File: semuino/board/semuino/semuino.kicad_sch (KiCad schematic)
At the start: 56 parts, among them J1 12V_POWER_IN, J10 POW LED 3, J11 RF ON/OFF, J12 Screen, J13 Earth humidity sensor, J14 Select, J2 Select, J3 12V_POWER_OUT, J4 5V_POWER_IN, J5 RGB 1, J6 RGB 2, J7 RGB 3, J8 POW LED 1, J9 POW LED 2, Q1 2N2222A, Q2 P03P4L-04, Q3 2N2222A, Q4 2N2222A, Q5 2N2222A, Q6 P03P4L-04, Q7 P03P4L-04, Q8 P03P4L-04, U1 RtcArduino, U2 BPC_ESP8266-01_ESP-01, U3 BPC_DHT22, U4 BPC_Alim3_3V

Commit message: Après nettoyage et vérification des règles
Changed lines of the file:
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@@
   (junction (at 39.37 19.05) (diameter 0) (color 0 0 0 0)
   )
+  (junction (at 52.07 19.05) (diameter 0) (color 0 0 0 0)
+  )
   (junction (at 250.19 115.57) (diameter 0) (color 0 0 0 0)
   )
@@
     (stroke (width 0) (type default))
   )
+  (wire (pts (xy 52.07 17.78) (xy 52.07 19.05))
+    (stroke (width 0) (type default))
+  )
   (wire (pts (xy 66.04 124.46) (xy 58.42 124.46))
     (stroke (width 0) (type default))
@@
     (stroke (width 0) (type default))
   )
+  (wire (pts (xy 52.07 19.05) (xy 77.47 19.05))
+    (stroke (width 0) (type default))
+  )
   (wire (pts (xy 58.42 109.22) (xy 66.04 109.22))
     (stroke (width 0) (type default))
@@
     (stroke (width 0) (type default))
   )
-  (wire (pts (xy 39.37 19.05) (xy 77.47 19.05))
+  (wire (pts (xy 39.37 19.05) (xy 52.07 19.05))
     (stroke (width 0) (type default))
   )
@@
         )
       )
+    )
+  )
+  (symbol (lib_id "power:PWR_FLAG") (at 52.07 17.78 0) (unit 1)
+    (in_bom yes) (on_board yes) (dnp no) (fields_autoplaced)
+    (property "Reference" "#FLG01" (at 52.07 15.875 0)
+      (effects (font (size 1.27 1.27)) hide)
+    )
+    (property "Value" "PWR_FLAG" (at 52.07 13.835 0)
+      (effects (font (size 1.27 1.27)))
+    )
+    (property "Footprint" "" (at 52.07 17.78 0)
+      (effects (font (size 1.27 1.27)) hide)
+    )
+    (property "Datasheet" "~" (at 52.07 17.78 0)
+      (effects (font (size 1.27 1.27)) hide)
+    )
+    (pin "1")
+    (instances
+      (project "semuino"
+        (path "/9b55b725-5036-433a-9024-8e2d1f50e0ac"
+          (reference "#FLG01") (unit 1)
+        )
+      )

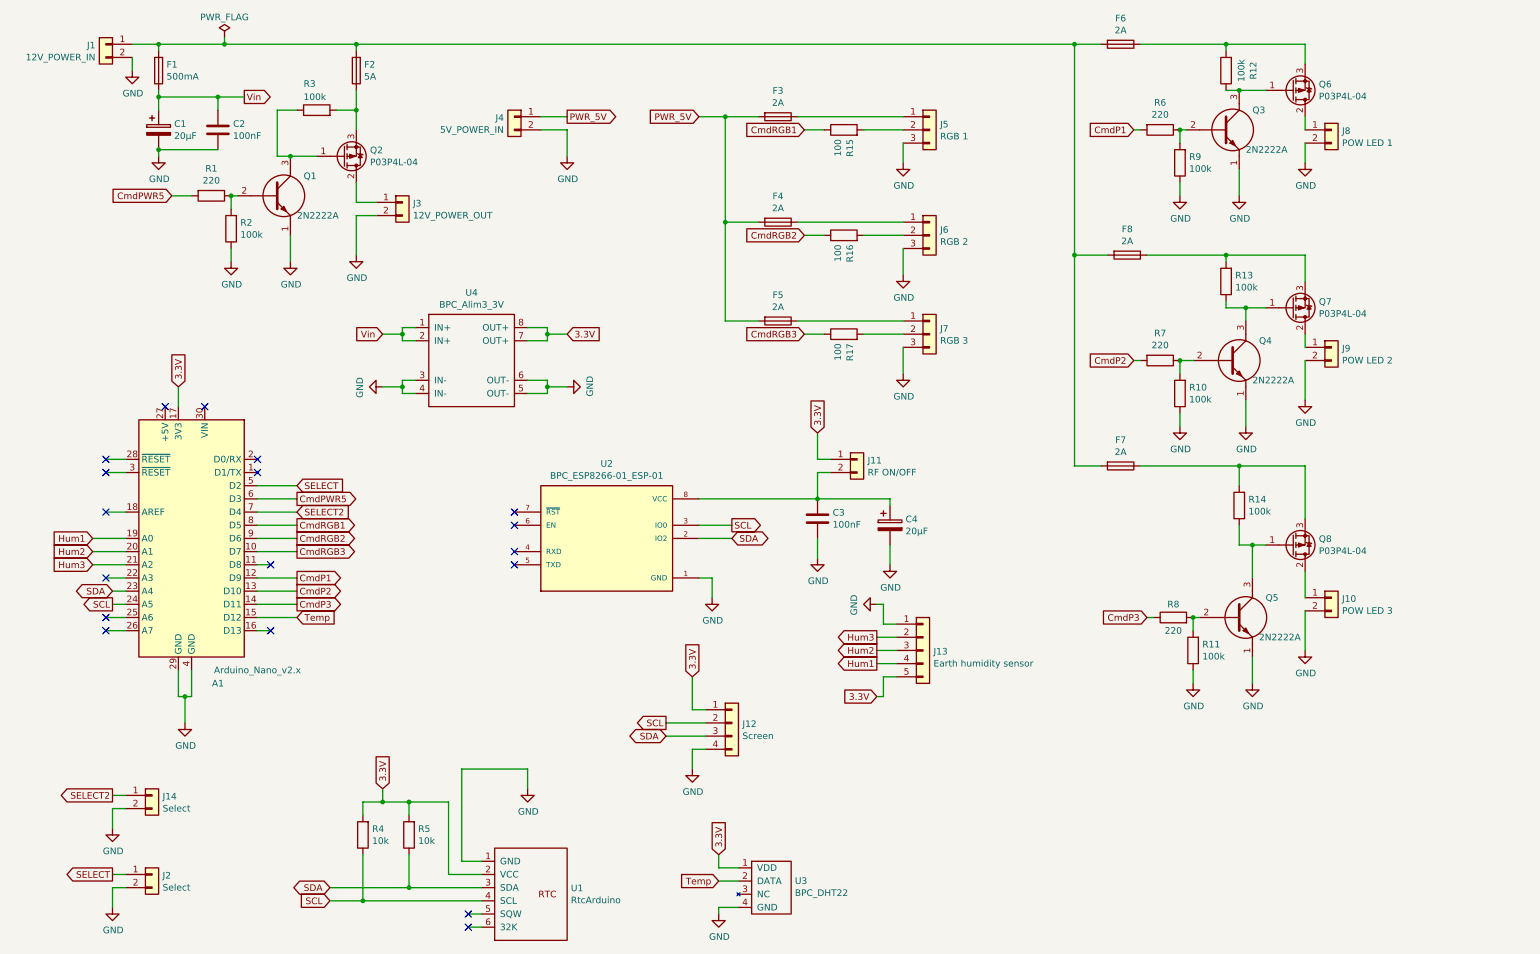
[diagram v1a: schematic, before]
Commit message: Modification valeur des résistances de commande + Marquage future A1
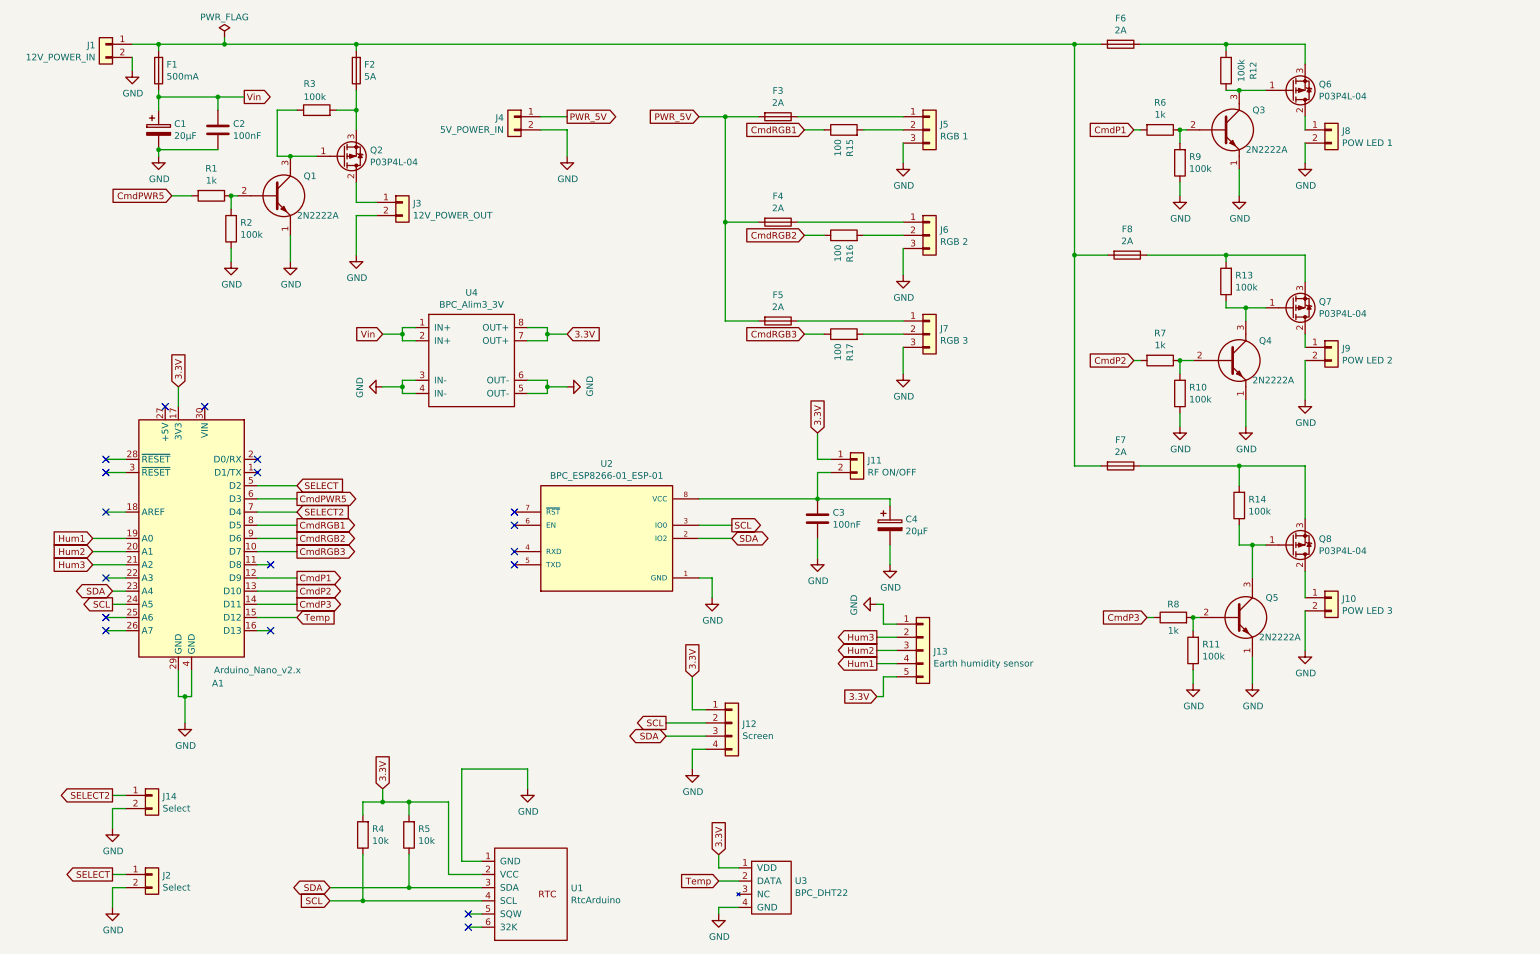
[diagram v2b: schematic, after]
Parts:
- R1, R6, R7, R8: value 220 -> 1k
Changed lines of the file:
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@@
   (title_block
     (title "Semuino - Contrôleur de meuble à semis")
-    (date "2023-09-21")
-    (rev "A0")
+    (date "2023-10-18")
+    (rev "A1")
     (company "BPC")
     (comment 2 "Température ambiante - 3 Capteurs d'humidité")
@@
       (effects (font (size 1.27 1.27)))
     )
-    (property "Value" "220" (at 232.41 32.6136 90)
+    (property "Value" "1k" (at 232.41 32.6136 90)
       (effects (font (size 1.27 1.27)))
     )
@@
       (effects (font (size 1.27 1.27)))
     )
-    (property "Value" "220" (at 232.41 77.0636 90)
+    (property "Value" "1k" (at 232.41 77.0636 90)
       (effects (font (size 1.27 1.27)))
     )
@@
       (effects (font (size 1.27 1.27)))
     )
-    (property "Value" "220" (at 234.95 132.08 90)
+    (property "Value" "1k" (at 234.95 132.08 90)
       (effects (font (size 1.27 1.27)))
     )
@@
       (effects (font (size 1.27 1.27)))
     )
-    (property "Value" "220" (at 49.53 45.3136 90)
-      (effects (font (size 1.27 1.27)))
-    )
+    (property "Value" "1k" (at 49.53 45.3136 90)
+      (effects (font (size 1.27 1.27)))
+    )

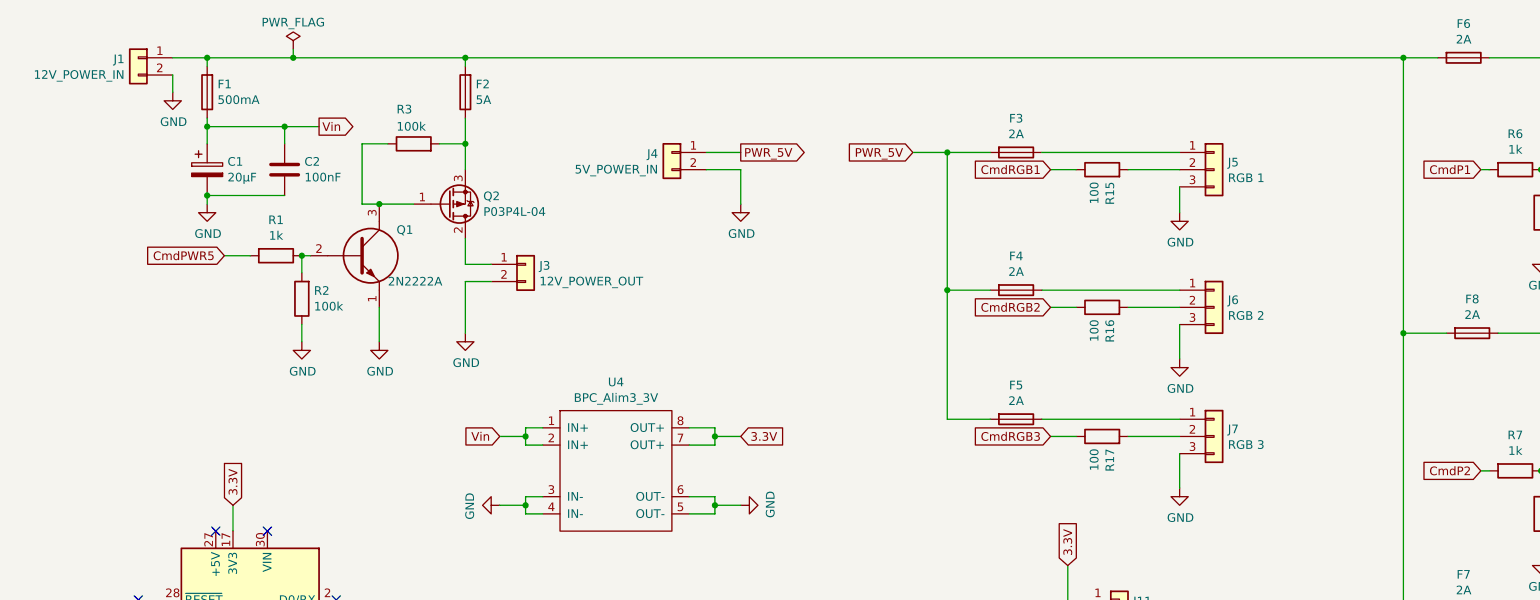
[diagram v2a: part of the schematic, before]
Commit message: Passage carte semuino en A2 avec résistances 0R et commentaires/annotations suite mise en service de A0
Petit loupé niveau alim du nano qui doit se faire sur la broche 5V et non 3.3 (qui est une sortie)
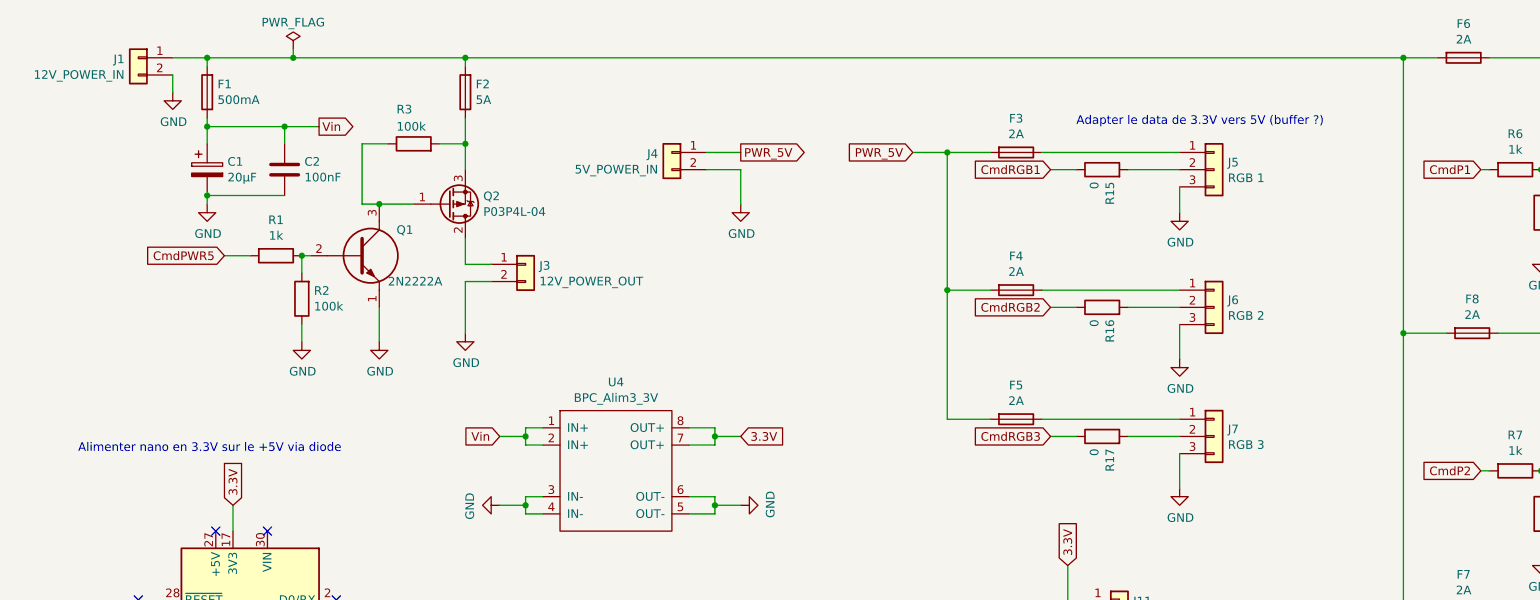
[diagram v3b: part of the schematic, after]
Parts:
- R15, R16, R17: value 100 -> 0
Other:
- note added: "Adapter le data de 3.3V vers 5V (buffer ?)"
- note added: "Alimenter nano en 3.3V sur le +5V via diode"
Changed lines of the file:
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@@
   (title_block
     (title "Semuino - Contrôleur de meuble à semis")
-    (date "2023-10-18")
-    (rev "A1")
+    (date "2023-12-22")
+    (rev "A2")
     (company "BPC")
     (comment 2 "Température ambiante - 3 Capteurs d'humidité")
@@
     (stroke (width 0) (type default))
   )
+  (text "Alimenter nano en 3.3V sur le +5V via diode" (at 20.32 77.47 0)
+    (effects (font (size 1.27 1.27)) (justify left bottom))
+  )
+  (text "Adapter le data de 3.3V vers 5V (buffer ?)" (at 167.64 29.21 0)
+    (effects (font (size 1.27 1.27)) (justify left bottom))
+  )
   (global_label "CmdRGB2" (shape output) (at 66.04 114.3 0)
     (effects (font (size 1.27 1.27)) (justify left))
@@
       (effects (font (size 1.27 1.27)) (justify right))
     )
-    (property "Value" "100" (at 170.307 37.338 0)
+    (property "Value" "0" (at 170.307 37.338 0)
       (effects (font (size 1.27 1.27)) (justify right))
     )
@@
       (effects (font (size 1.27 1.27)) (justify right))
     )
-    (property "Value" "100" (at 170.307 57.658 0)
+    (property "Value" "0" (at 170.307 57.658 0)
       (effects (font (size 1.27 1.27)) (justify right))
     )
@@
       (effects (font (size 1.27 1.27)) (justify right))
     )
-    (property "Value" "100" (at 170.307 76.708 0)
+    (property "Value" "0" (at 170.307 76.708 0)
       (effects (font (size 1.27 1.27)) (justify right))
     )

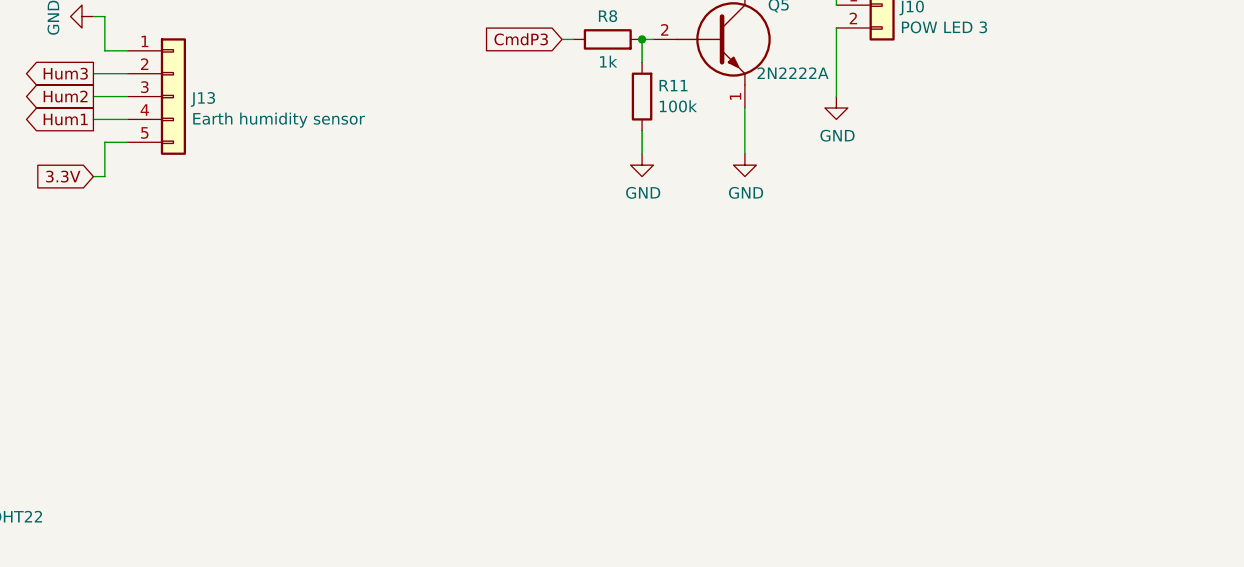
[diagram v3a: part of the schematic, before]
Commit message: Ajout d'un warning sur le schéma pour indiquer que l'alimentation 5V doit être filtrée pour éviter les perturbations.
Sinon les RGBs ne fonctionnent pas
Plus tard, cette capa pourrait être intégrée à la carte ?
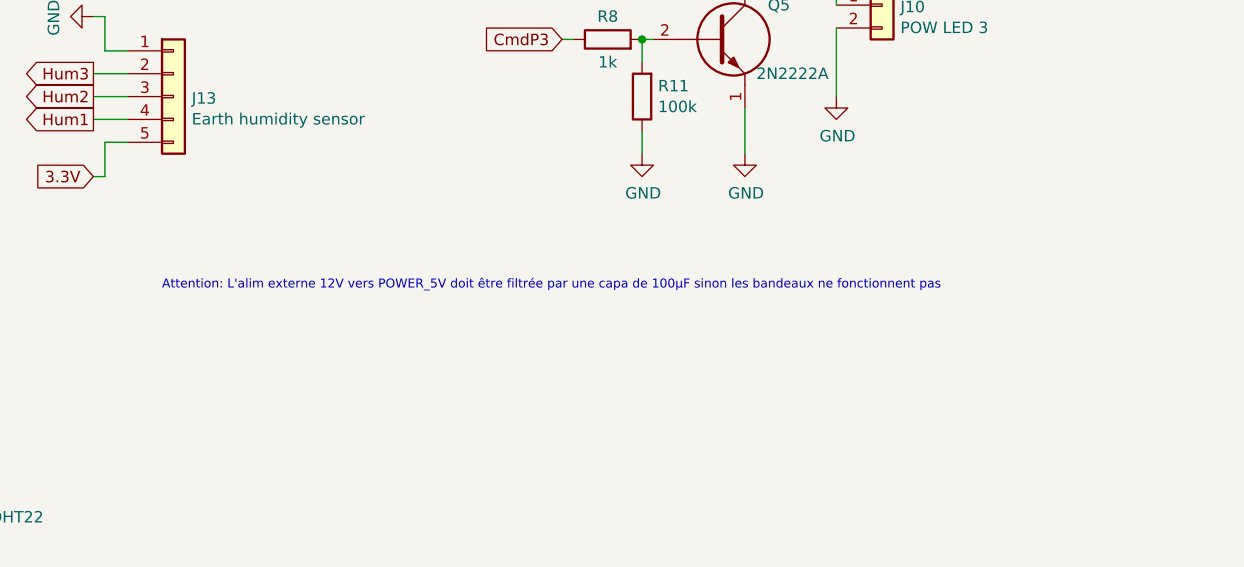
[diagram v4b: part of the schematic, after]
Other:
- note added: "Attention: L'alim externe 12V vers POWER_5V doit être filtrée par une capa de 100µF sinon les bandeaux ne fonctionnent pas"
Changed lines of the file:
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@@
     (effects (font (size 1.27 1.27)) (justify left bottom))
+  )
+  (text "Attention: L'alim externe 12V vers POWER_5V doit être filtrée par une capa de 100µF sinon les bandeaux ne fonctionnent pas"
+    (at 185.42 157.48 0)
+    (effects (font (size 1 1)) (justify left bottom))
   )
   (global_label "CmdRGB2" (shape output) (at 66.04 114.3 0)
